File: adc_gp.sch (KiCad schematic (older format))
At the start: 85 parts, among them IC3 ADS8686SIPZAR

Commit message: layout cleanup; removed custom footrpints
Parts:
- IC3: footprint covg-kicad:QFP65P1600X1600X160-80N -> Package_QFP:LQFP-80_14x14mm_P0.65mm
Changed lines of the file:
@@
 F 0 "IC3" H 7650 2700 50  0000 L CNN
 F 1 "ADS8686SIPZAR" H 7450 2600 50  0000 L CNN
-F 2 "covg-kicad:QFP65P1600X1600X160-80N" H 8750 4200 50  0001 L CNN
+F 2 "Package_QFP:LQFP-80_14x14mm_P0.65mm" H 8750 4200 50  0001 L CNN
 F 3 "https://www.ti.com/lit/gpn/ADS8686S" H 8750 4100 50  0001 L CNN
 F 4 "Analog to Digital Converters - ADC 16-channel 16-bit 1-MSPS dual simultaneous-sampling ADC with integrated analog front end (AFE)" H 8750 4000 50  0001 L CNN "Description"

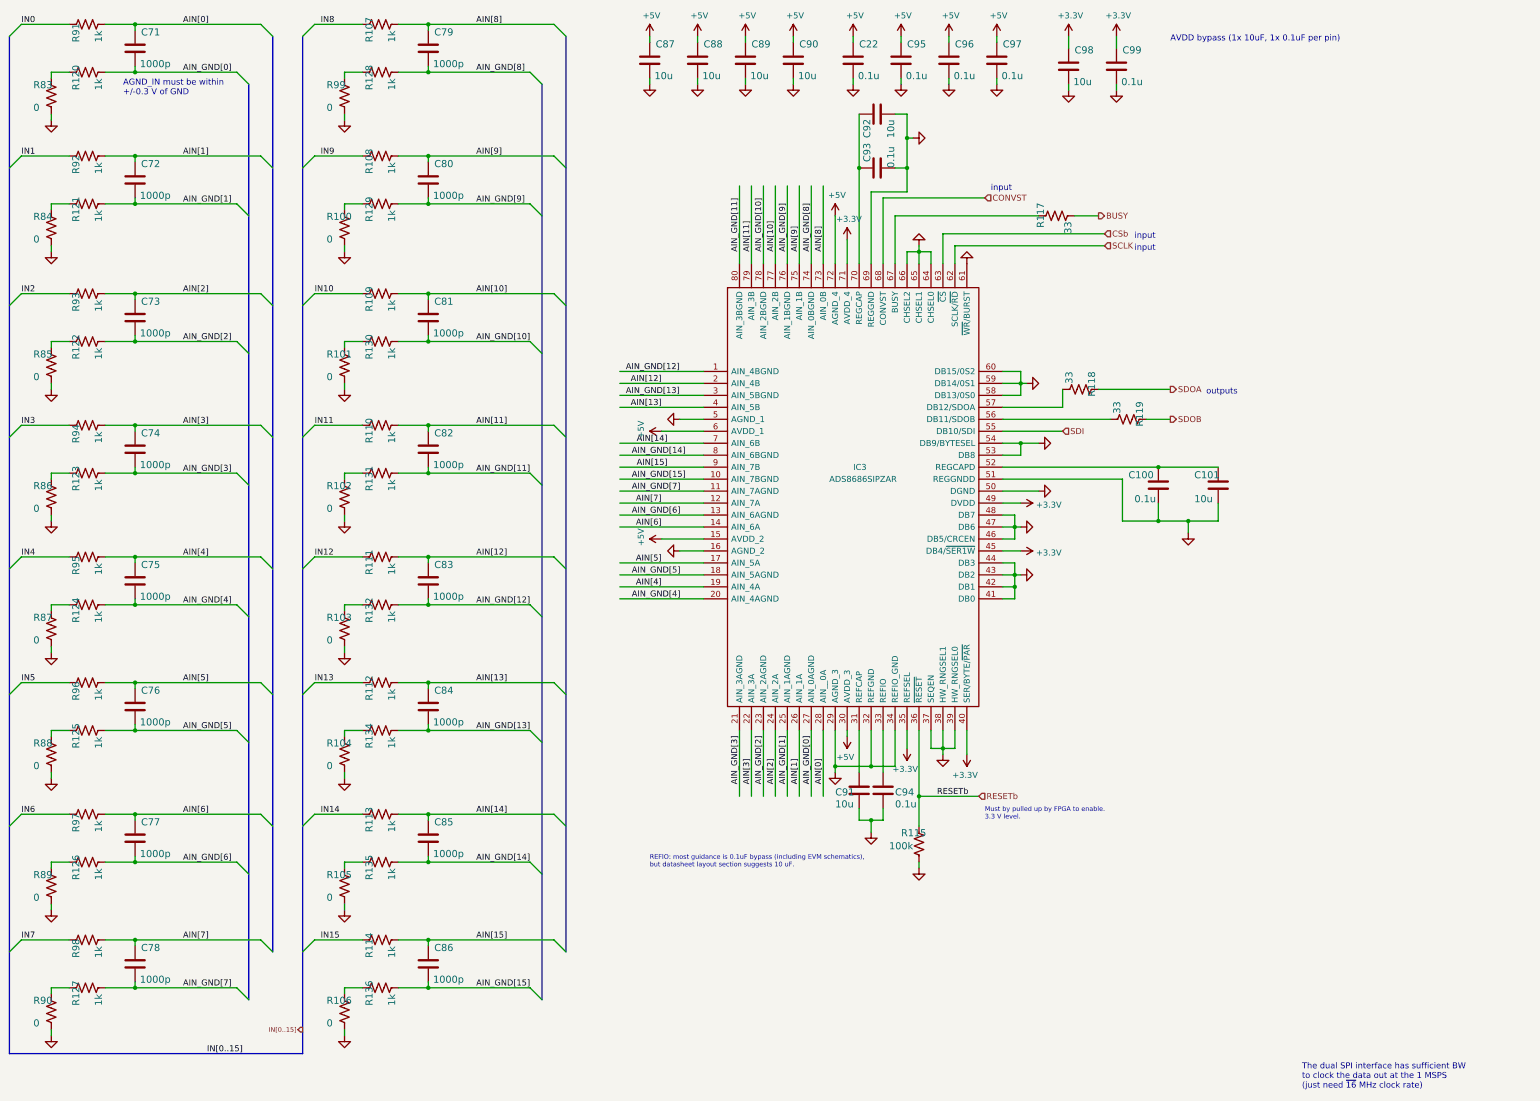
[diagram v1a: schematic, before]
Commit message: updates of DAC part placement
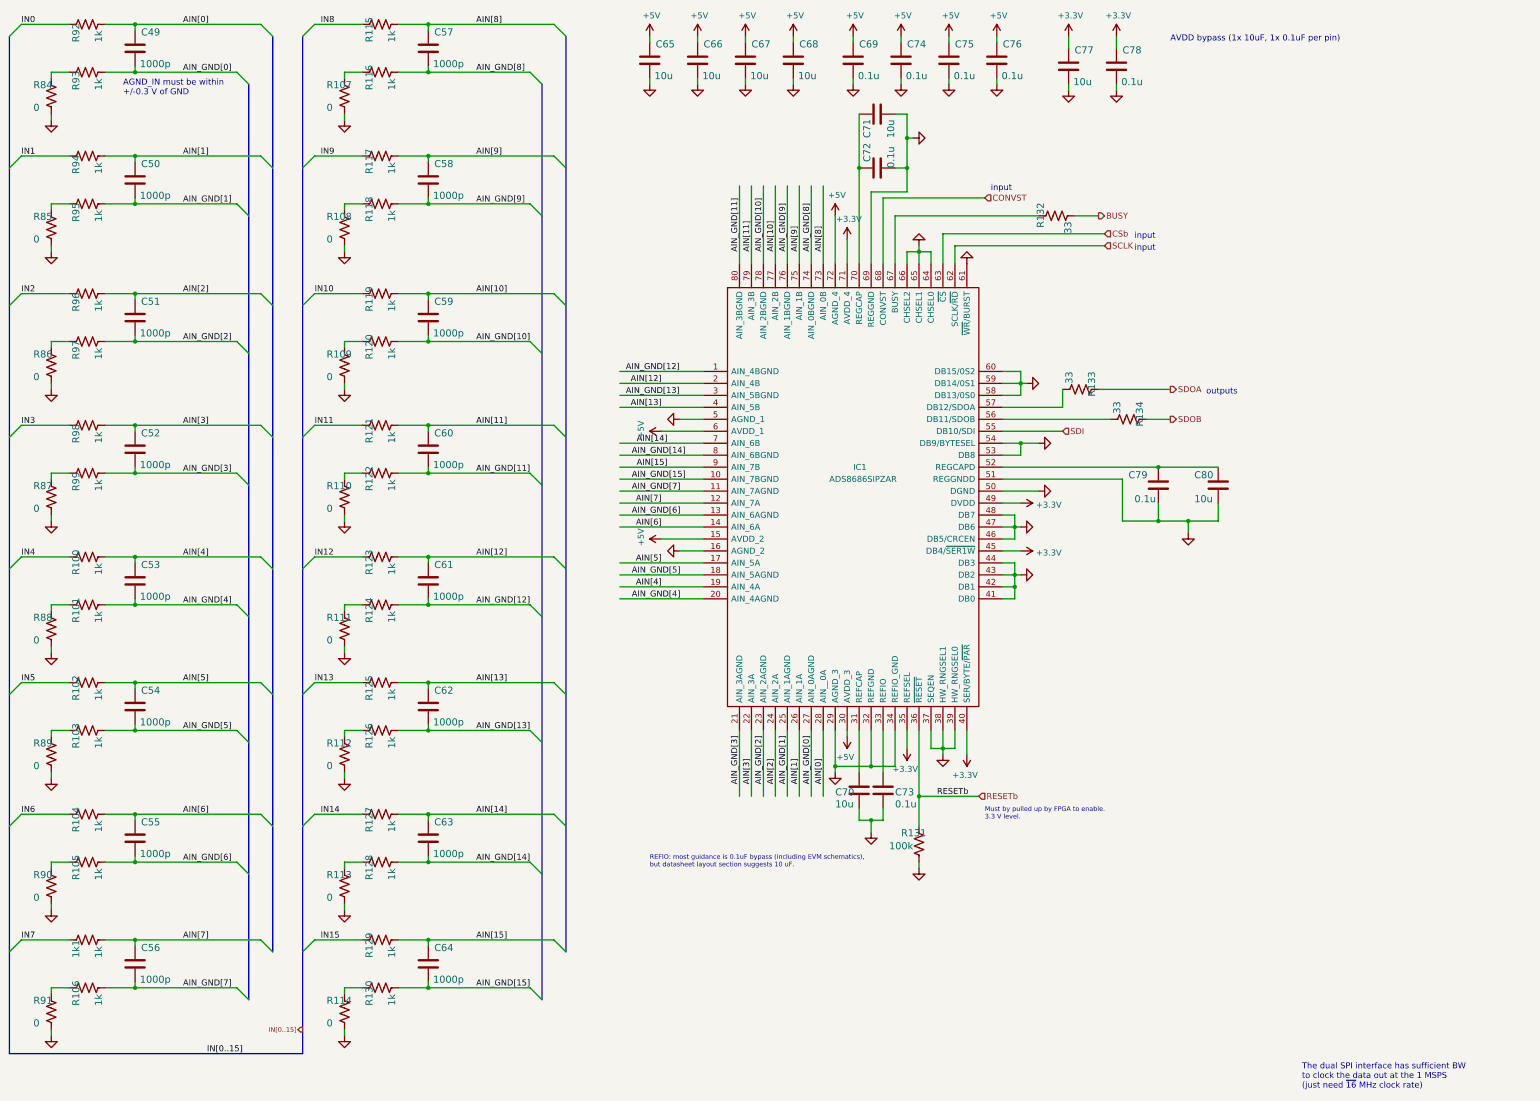
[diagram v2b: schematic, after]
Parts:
- renumbered R98 to 1k1, C71 to C49, C72 to C50, C73 to C51, C74 to C52, C75 to C53, C76 to C54, C77 to C55, C78 to C56, C79 to C57, C80 to C58, C81 to C59, C82 to C60, C83 to C61, C84 to C62, C85 to C63, C86 to C64, C87 to C65, C88 to C66, C89 to C67, C90 to C68, C22 to C69, C91 to C70, C92 to C71, C93 to C72, C94 to C73, C95 to C74, C96 to C75, C97 to C76, C98 to C77, C99 to C78, C100 to C79, C101 to C80, IC3 to IC1, R95 to R100, R124 to R101, R96 to R102, R125 to R103, R97 to R104, R126 to R105, R127 to R106, R99 to R107, R100 to R108, R101 to R109, R102 to R110, R103 to R111, R104 to R112, R105 to R113, R106 to R114, R107 to R115, R128 to R116, R108 to R117, R129 to R118, R109 to R119, R130 to R120, R110 to R121, R131 to R122, R111 to R123, R132 to R124, R112 to R125, R134 to R126, R113 to R127, R135 to R128, R114 to R129, R136 to R130, R115 to R131, R117 to R132, R118 to R133, R119 to R134, R83 to R84, R84 to R85, R85 to R86, R86 to R87, R87 to R88, R88 to R89, R89 to R90, R90 to R91, R91 to R92, R120 to R93, R92 to R94, R121 to R95, R93 to R96, R122 to R97, R94 to R98, R123 to R99

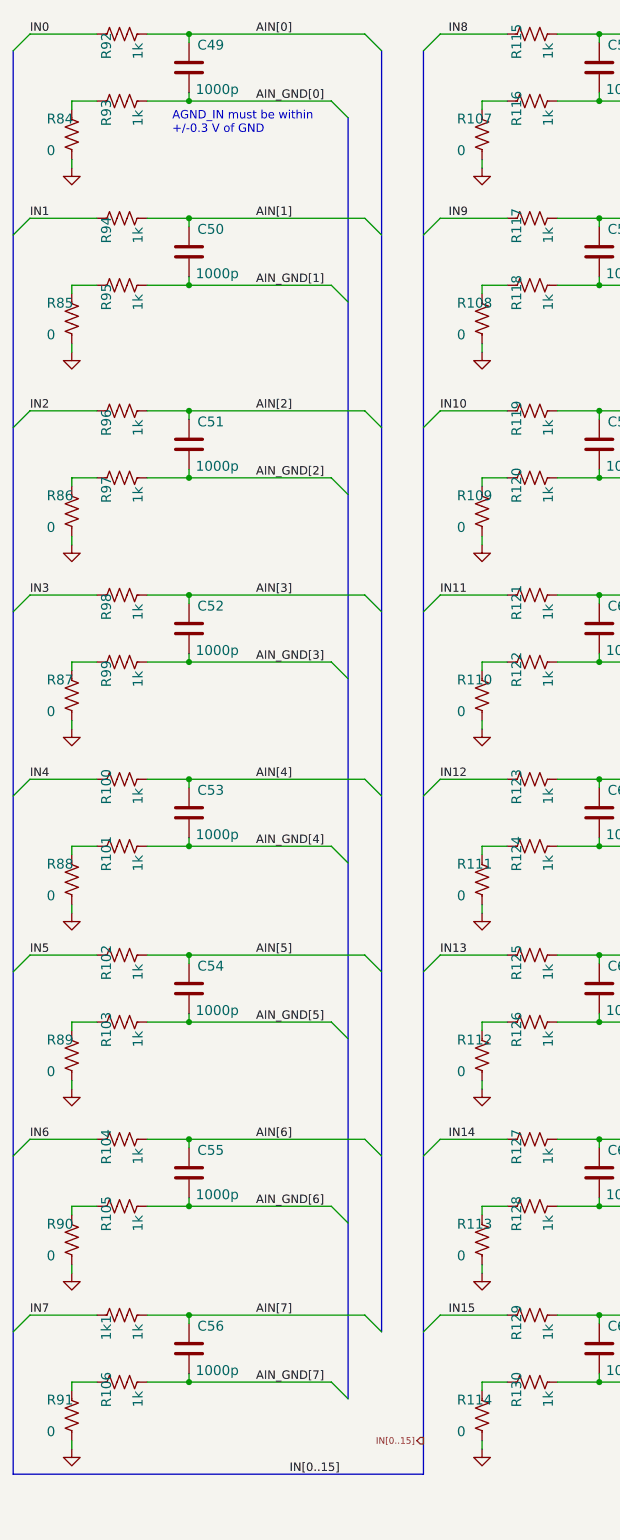
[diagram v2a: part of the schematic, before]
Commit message: updated component placement
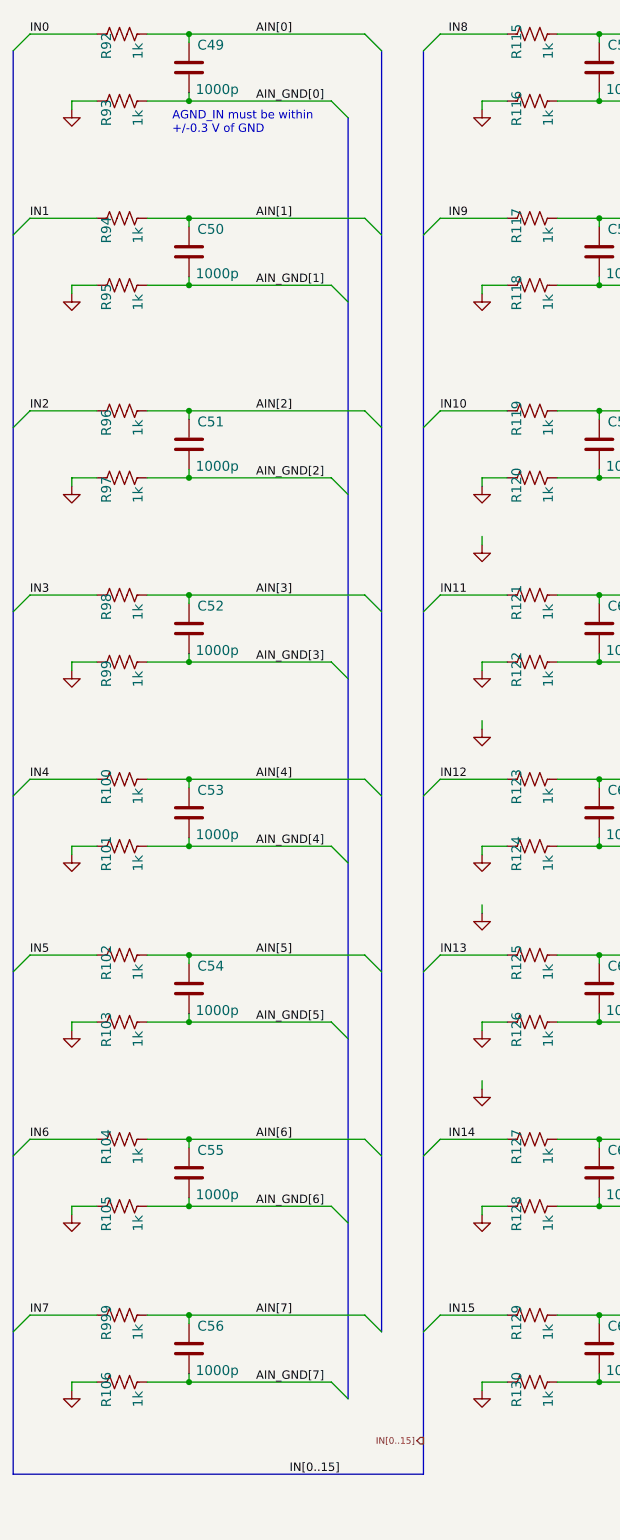
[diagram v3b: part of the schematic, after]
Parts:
- removed R107, R108, R109, R110, R111, R112, R113, R114, R84, R85, R86, R87, R88, R89, R90, R91: 0, Resistor_SMD:R_0603_1608Metric, symbol Device:R_US
- renumbered 1k1 to R999
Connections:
- wire segments 312 -> 300

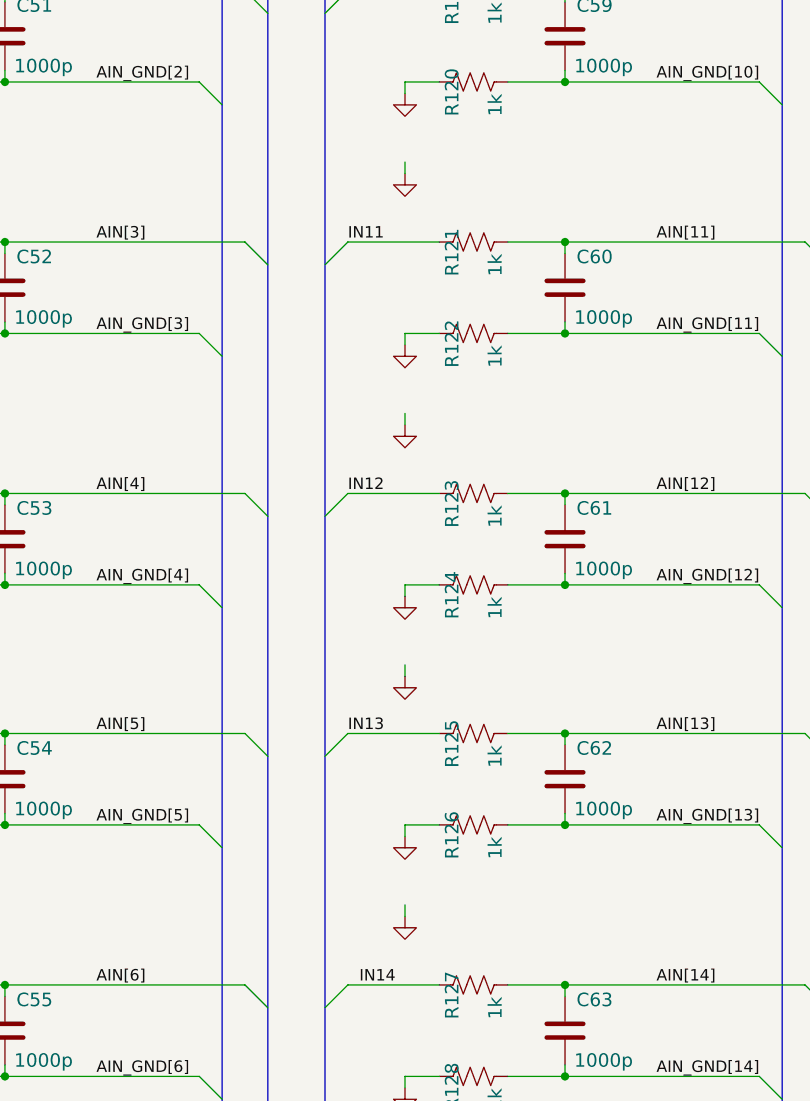
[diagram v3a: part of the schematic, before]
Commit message: completing gp DAC layout
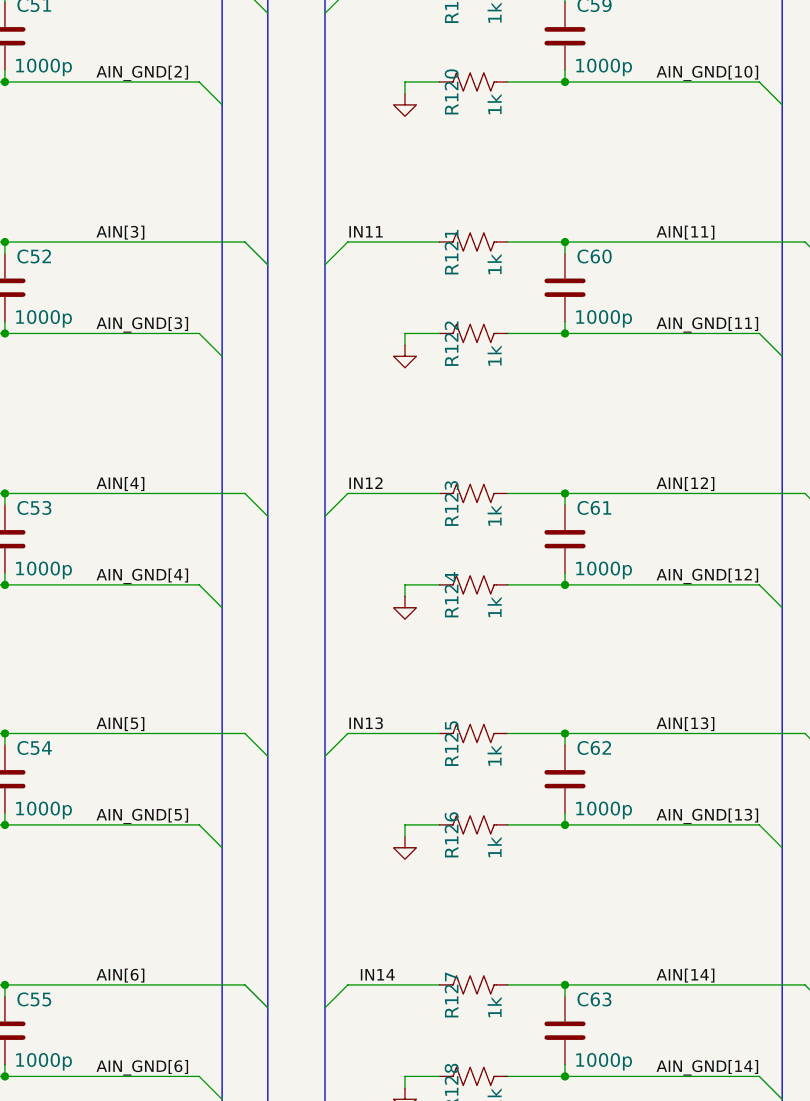
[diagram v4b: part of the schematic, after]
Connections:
- wire segments 300 -> 296
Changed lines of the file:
@@
 $Descr User 13023 9707
 encoding utf-8
-Sheet 7 18
+Sheet 7 26
 Title ""
 Date ""
@@
 $EndComp
 $Comp
-L power:GND #GND?
-U 1 1 6152B64A
-P 3400 6900
-AR Path="/6152B64A" Ref="#GND?"  Part="1"
-AR Path="/6095A004/6152B64A" Ref="#GND0102"  Part="1"
-F 0 "#GND0102" H 3400 6900 50  0001 C CNN
-F 1 "GND" H 3300 6800 59  0001 L BNN
-F 2 "" H 3400 6900 50  0001 C CNN
-F 3 "" H 3400 6900 50  0001 C CNN
-	1    3400 6900
-	1    0    0    -1
-$EndComp
-$Comp
 L Device:C C?
 U 1 1 6152B665
@@
 $EndComp
 $Comp
-L power:GND #GND?
-U 1 1 6152B676
-P 3400 5850
-AR Path="/6152B676" Ref="#GND?"  Part="1"
-AR Path="/6095A004/6152B676" Ref="#GND0101"  Part="1"
-F 0 "#GND0101" H 3400 5850 50  0001 C CNN
-F 1 "GND" H 3300 5750 59  0001 L BNN
-F 2 "" H 3400 5850 50  0001 C CNN
-F 3 "" H 3400 5850 50  0001 C CNN
-	1    3400 5850
-	1    0    0    -1
-$EndComp
-$Comp
 L Device:C C?
 U 1 1 6152B691
@@
 $EndComp
 $Comp
-L power:GND #GND?
-U 1 1 6152B6A2
-P 3400 4750
-AR Path="/6152B6A2" Ref="#GND?"  Part="1"
-AR Path="/6095A004/6152B6A2" Ref="#GND0100"  Part="1"
-F 0 "#GND0100" H 3400 4750 50  0001 C CNN
-F 1 "GND" H 3300 4650 59  0001 L BNN
-F 2 "" H 3400 4750 50  0001 C CNN
-F 3 "" H 3400 4750 50  0001 C CNN
-	1    3400 4750
-	1    0    0    -1
-$EndComp
-$Comp
 L Device:C C?
 U 1 1 6152B6BD
@@
 	1    3700 2850
 	0    -1   -1   0
-$EndComp
-$Comp
-L power:GND #GND?
-U 1 1 6152B6CE
-P 3400 3650
-AR Path="/6152B6CE" Ref="#GND?"  Part="1"
-AR Path="/6095A004/6152B6CE" Ref="#GND099"  Part="1"
-F 0 "#GND099" H 3400 3650 50  0001 C CNN
-F 1 "GND" H 3300 3550 59  0001 L BNN
-F 2 "" H 3400 3650 50  0001 C CNN
-F 3 "" H 3400 3650 50  0001 C CNN
-	1    3400 3650
-	1    0    0    -1
 $EndComp
 $Comp
@@
 	4100 6100 3850 6100
 Wire Wire Line
-	3400 6900 3400 6850
-Wire Wire Line
 	3400 6550 3400 6500
 Wire Wire Line
@@
 	4100 5050 3850 5050
 Wire Wire Line
-	3400 5850 3400 5800
-Wire Wire Line
 	3400 5500 3400 5450
 Wire Wire Line
@@
 	4100 3950 3850 3950
 Wire Wire Line
-	3400 4750 3400 4700
-Wire Wire Line
 	3400 4400 3400 4350
 Wire Wire Line
@@
 	4100 2850 3850 2850
 Wire Wire Line
-	3400 3650 3400 3600
-Wire Wire Line
 	3400 3300 3400 3250

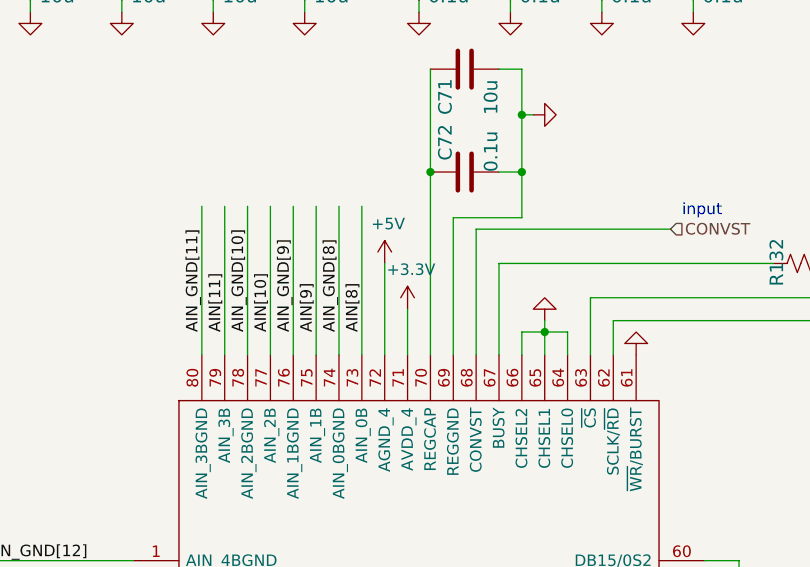
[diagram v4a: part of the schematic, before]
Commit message: updates after bug in ADS8686 power connectivity. And swap of DC SCL and SDA
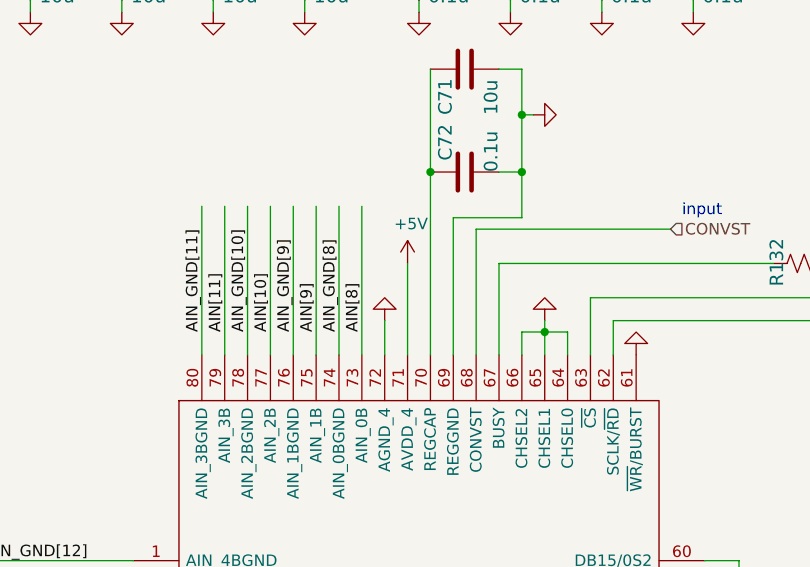
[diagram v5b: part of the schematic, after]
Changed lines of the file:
@@
 $Descr User 13023 9707
 encoding utf-8
-Sheet 7 26
+Sheet 11 26
 Title ""
 Date ""
@@
 L power:+5V #PWR0143
 U 1 1 60F8A03B
-P 7500 2200
-F 0 "#PWR0143" H 7500 2050 50  0001 C CNN
-F 1 "+5V" H 7515 2373 50  0000 C CNN
-F 2 "" H 7500 2200 50  0001 C CNN
-F 3 "" H 7500 2200 50  0001 C CNN
-	1    7500 2200
+P 7600 2200
+F 0 "#PWR0143" H 7600 2050 50  0001 C CNN
+F 1 "+5V" H 7615 2373 50  0000 C CNN
+F 2 "" H 7600 2200 50  0001 C CNN
+F 3 "" H 7600 2200 50  0001 C CNN
+	1    7600 2200
 	1    0    0    -1
 $EndComp
@@
 	1    8150 1550
 	0    -1   -1   0
-$EndComp
-$Comp
-L power:+3.3V #PWR0144
-U 1 1 614CCEA4
-P 7600 2400
-F 0 "#PWR0144" H 7600 2250 50  0001 C CNN
-F 1 "+3.3V" H 7615 2573 50  0000 C CNN
-F 2 "" H 7600 2400 50  0001 C CNN
-F 3 "" H 7600 2400 50  0001 C CNN
-	1    7600 2400
-	1    0    0    -1
 $EndComp
 $Comp
@@
 	6050 4000 6400 4000
 Wire Wire Line
-	7500 2200 7500 2600
-Wire Wire Line
 	1400 8650 1650 8650
 Wire Wire Line
@@
 Wire Wire Line
 	7400 1950 7400 2600
-Wire Wire Line
-	7600 2400 7600 2600
 Wire Wire Line
 	3850 8650 4100 8650
@@
 Wire Wire Line
 	950  4350 950  4400
+Wire Wire Line
+	7600 2200 7600 2600
+$Comp
+L power:GND #GND?
+U 1 1 610F8B76
+P 7500 2450
+AR Path="/610F8B76" Ref="#GND?"  Part="1"
+AR Path="/6095A004/610F8B76" Ref="#GND?"  Part="1"
+F 0 "#GND?" H 7500 2450 50  0001 C CNN
+F 1 "GND" H 7400 2350 59  0001 L BNN
+F 2 "" H 7500 2450 50  0001 C CNN
+F 3 "" H 7500 2450 50  0001 C CNN
+	1    7500 2450
+	-1   0    0    1
+$EndComp
+Wire Wire Line
+	7500 2450 7500 2600
 Wire Bus Line
 	2600 1100 2600 8750

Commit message: DC-DC Regulator updated
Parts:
- C49, C50, C51, C52, C53, C54, C55, C56, C57, C58, C59, C60, C61, C62, C63, C64, C65, C66, C67, C68, C69, C70, C71, C72, C73, C74, C75, C76, C77, C78, C79, C80: symbol Device:C -> covg_daq_v2-rescue:C-Device
- IC1: symbol covg-kicad:ADS8686SIPZAR -> covg_daq_v2-rescue:ADS8686SIPZAR-covg-kicad
- R100, R101, R102, R103, R104, R105, R106, R115, R116, R117, R118, R119, R120, R121, R122, R123, R124, R125, R126, R127, R128, R129, R130, R131, R132, R133, R134, R92, R93, R94, R95, R96, R97, R98, R99, R999: symbol Device:R_US -> covg_daq_v2-rescue:R_US-Device

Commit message: rolled back to commit b6c4f66 because of rescue libraries
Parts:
- C49, C50, C51, C52, C53, C54, C55, C56, C57, C58, C59, C60, C61, C62, C63, C64, C65, C66, C67, C68, C69, C70, C71, C72, C73, C74, C75, C76, C77, C78, C79, C80: symbol covg_daq_v2-rescue:C-Device -> Device:C
- IC1: symbol covg_daq_v2-rescue:ADS8686SIPZAR-covg-kicad -> covg-kicad:ADS8686SIPZAR
- R100, R101, R102, R103, R104, R105, R106, R115, R116, R117, R118, R119, R120, R121, R122, R123, R124, R125, R126, R127, R128, R129, R130, R131, R132, R133, R134, R92, R93, R94, R95, R96, R97, R98, R99, R999: symbol covg_daq_v2-rescue:R_US-Device -> Device:R_US
